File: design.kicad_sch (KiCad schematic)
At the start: 274 parts, among them J1 TYPE-C-31-M-12, U1 TTP223, U10 ATtiny1616-M, U2 TTP223, U3 TTP223, U4 TTP223, U5 TTP223, U6 TTP223, U7 TTP223, U8 TTP223, U9 MAX77751CEFG_T

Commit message: new layout
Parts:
- removed D301, D302, D303, D304, D305, D306, D307, D308, D309, D310, D311, D312, D313, D314, D315, D316, D317, D318, D319, D320, D321, D322, D323, D324, D325, D326, D327, D328, D329, D330, D331, D332, D333, D334, D335, D336, D337, D338, D339, D340, D341, D342, D343, D344, D345, D346, D347, D348, D349, D350, D351, D352, D353, D354, D355, D356, D357, D358, D359, D360, D361, D362, D363, D364, D365, D366, D367, D368, D369, D370, D371, D372, D373, D374, D375, D376, D377, D378, D379, D380, D381, D382, D383, D384, D385, D386, D387, D388, D389, D390, D391, D392, D393, D394, D395, D396: WS2812B, LED_SMD:LED_WS2812B_PLCC4_5.0x5.0mm_P3.2mm, symbol LED:WS2812B

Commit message: updates
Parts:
- added J301: TYPE-C-31-M-12, Snapeda:TYPE-C-31-M-12_HRO_TYPE-C-31-M-12, symbol Snapeda:TYPE-C-31-M-12
- added R301, R302: 5.1k, Resistor_SMD:R_0805_2012Metric, symbol Device:R_Small
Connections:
- net +5V: now also J301.A4_B9 (VBUS), J301.B4_A9 (VBUS)
- net GND: now also J301.A1_B12 (GND), J301.B1_A12 (GND), R301.1, R302.2
- net in: now also U10.5 (PA4); no longer U10.1 (PA2)
- net touch_point_1: no longer U10.7 (PA6)
- net touch_point_2: no longer U10.8 (PA7)
- net touch_point_3: no longer U10.14 (PB0)
- net touch_point_4: no longer U10.13 (PB1)
- net touch_point_5: no longer U10.12 (PB2)
- net touch_point_6: no longer U10.11 (PB3)
- net touch_point_7: no longer U10.10 (PB4)
- net touch_point_8: no longer U10.9 (PB5)
- net touch_state_1: now also U10.18 (PC3)
- net touch_state_2: now also U10.17 (PC2)
- net touch_state_3: now also U10.16 (PC1)
- net touch_state_4: now also U10.15 (PC0)
- net touch_state_5: now also U10.11 (PB3)
- net touch_state_6: now also U10.10 (PB4)
- net touch_state_7: now also U10.9 (PB5)
- net touch_state_8: now also U10.8 (PA7)
- net at R9.1: now also U10.6 (PA5); no longer U10.15 (PC0)
- net at R10.1: now also U10.7 (PA6); no longer U10.16 (PC1)
- new net: J301.A5 (CC1), R301.2
- new net: J301.B5 (CC2), R302.1
- new net: J301.S1 (SHIELD), J301.S2 (SHIELD), J301.S3 (SHIELD), J301.S4 (SHIELD)
- no-connect marks 9 -> 12
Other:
- moved on the sheet: D101, D102, R10, R9

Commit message: upadte
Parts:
- removed C17, C18, C19, C22: 10uF, Capacitor_SMD:C_0805_2012Metric, symbol Device:C_Small
- removed C20, C24, C25: 2.2uF, Capacitor_SMD:C_0805_2012Metric, symbol Device:C_Small
- removed C21: 0.1uF, Capacitor_SMD:C_0805_2012Metric, symbol Device:C_Small
- removed C23: 22uF, Capacitor_SMD:C_0805_2012Metric, symbol Device:C_Small
- removed D100: STAT, LED_SMD:LED_0603_1608Metric, symbol Device:LED_Small
- removed D98: VBUS, LED_SMD:LED_0603_1608Metric, symbol Device:LED_Small
- removed D99: INOKB, LED_SMD:LED_0603_1608Metric, symbol Device:LED_Small
- removed J1: TYPE-C-31-M-12, Snapeda:TYPE-C-31-M-12_HRO_TYPE-C-31-M-12, symbol Snapeda:TYPE-C-31-M-12
- removed JP17: ENBST, LED_SMD:LED_0603_1608Metric, symbol Jumper:Jumper_2_Bridged
- removed L1: 0.47uH, Inductor_SMD:L_0805_2012Metric, symbol Device:L_Small
- removed R2, R3, R5: 1k, Resistor_SMD:R_0805_2012Metric, symbol Device:R_Small
- removed R4, R6: 5.1k, Resistor_SMD:R_0805_2012Metric, symbol Device:R_Small
- removed R7: 2.4k, Resistor_SMD:R_0805_2012Metric, symbol Device:R_Small
- removed R8: 13.3k, Resistor_SMD:R_0805_2012Metric, symbol Device:R_Small
- removed TP10: BAT-, TestPoint:TestPoint_Pad_4.0x4.0mm, symbol Connector:TestPoint
- removed TP9: BAT+, TestPoint:TestPoint_Pad_4.0x4.0mm, symbol Connector:TestPoint
- removed U9: MAX77751CEFG_T, Snapeda:IC_MAX77751CEFG_T, symbol Snapeda:MAX77751CEFG_T
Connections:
- no-connect marks 12 -> 9
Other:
- note removed: "If ENBST is driven high, the reverse boost is enabled and the BYP-to-CHGIN path is closed. internall pulldown"
- note removed: "RESISTANCE (kΩ) IFAST (mA) 2.4 500 RTOPOFF (kΩ) ITOPOFF (mA) 13.3 200"
- moved on the sheet: D97, R1

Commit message: added lcsc number test
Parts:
- D1: LCSC (none) -> C123456
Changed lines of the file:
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@@
       (effects (font (size 1.27 1.27)) (justify left top) hide)
+    )
+    (property "LCSC" "C123456" (id 4) (at 369.57 41.91 0)
+      (effects (font (size 1.27 1.27)) hide)
     )
     (pin "1")

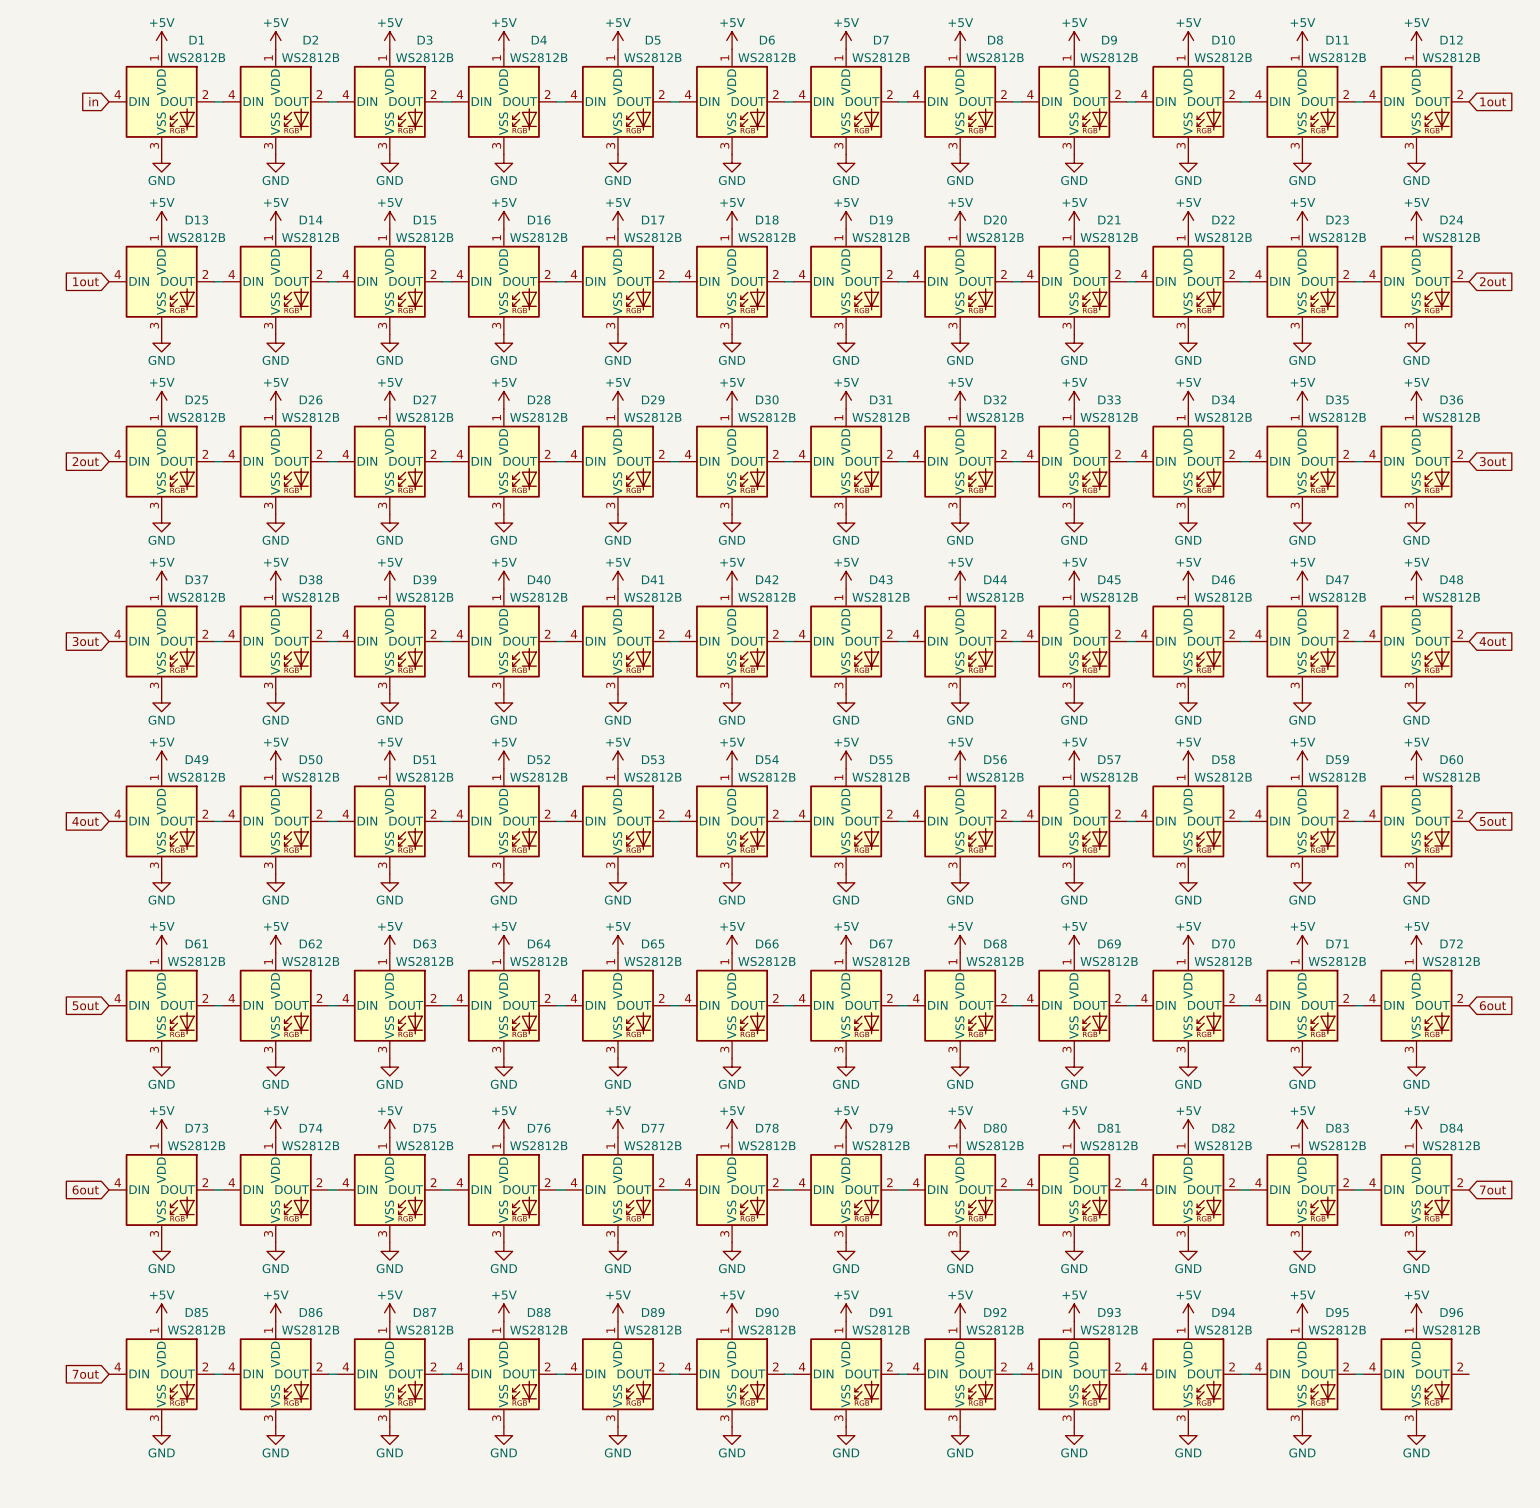
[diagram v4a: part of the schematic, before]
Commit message: update all LEDs with LCSC #
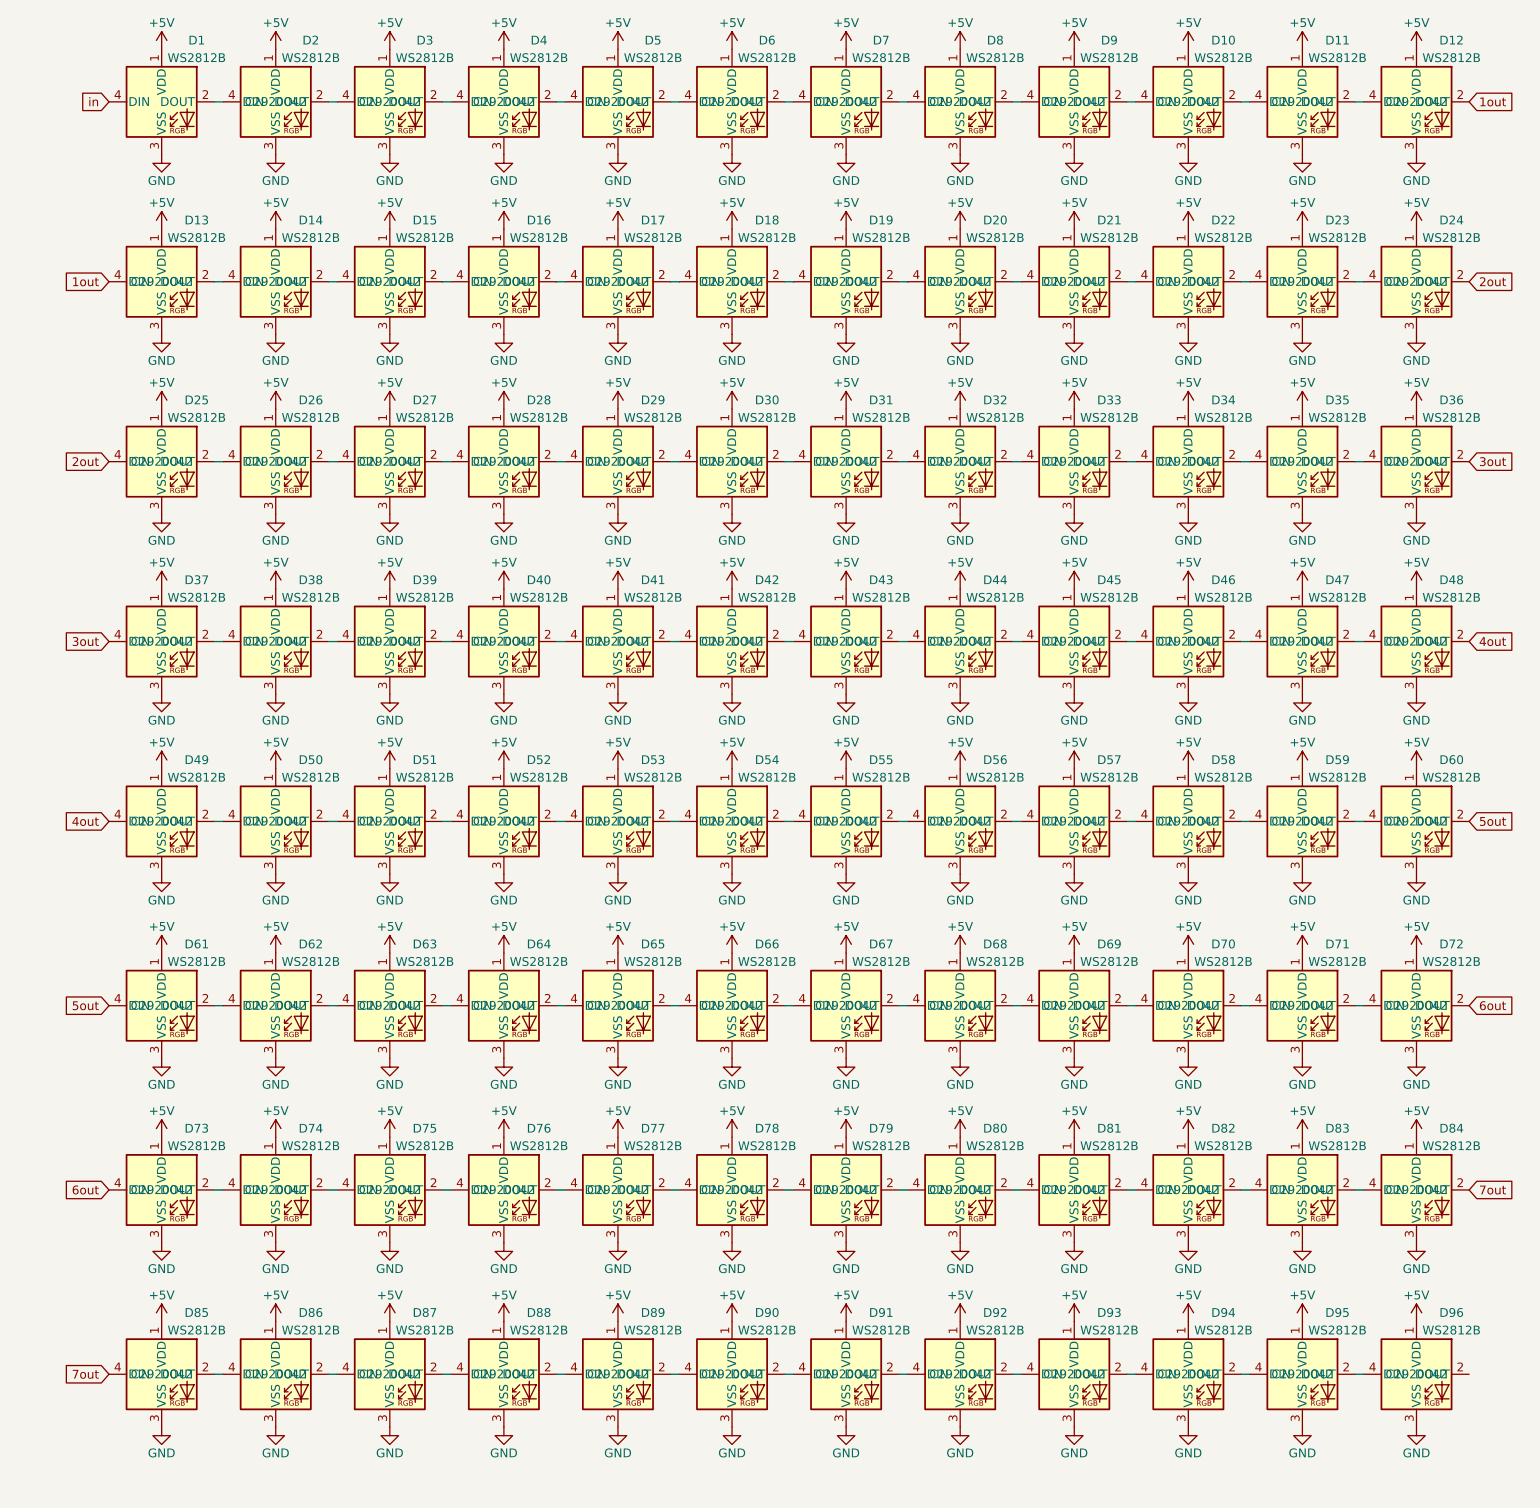
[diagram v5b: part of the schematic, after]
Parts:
- D1: LCSC C123456 -> C2920042
- D10, D11, D12, D13, D14, D15, D16, D17, D18, D19, D2, D20, D21, D22, D23, D24, D25, D26, D27, D28, D29, D3, D30, D31, D32, D33, D34, D35, D36, D37, D38, D39, D4, D40, D41, D42, D43, D44, D45, D46, D47, D48, D49, D5, D50, D51, D52, D53, D54, D55, D56, D57, D58, D59, D6, D60, D61, D62, D63, D64, D65, D66, D67, D68, D69, D7, D70, D71, D72, D73, D74, D75, D76, D77, D78, D79, D8, D80, D81, D82, D83, D84, D85, D86, D87, D88, D89, D9, D90, D91, D92, D93, D94, D95, D96: LCSC (none) -> C2920042

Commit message: update
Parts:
- added TP301: UPDI, TestPoint:TestPoint_Pad_3.0x3.0mm, symbol Connector:TestPoint
- added TP302: +5V, TestPoint:TestPoint_Pad_3.0x3.0mm, symbol Connector:TestPoint
- added TP303: GND, TestPoint:TestPoint_Pad_3.0x3.0mm, symbol Connector:TestPoint
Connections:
- net +5V: now also TP302.1
- net GND: now also TP303.1
- net UPDI: now also TP301.1
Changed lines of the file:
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@@
     (stroke (width 0) (type default) (color 0 0 0 0))
   )
+  (wire (pts (xy 485.14 292.735) (xy 485.14 295.275))
+    (stroke (width 0) (type default) (color 0 0 0 0))
+  )
   (wire (pts (xy 459.74 41.91) (xy 461.01 41.91))
     (stroke (width 0) (type default) (color 0 0 0 0))
@@
     (stroke (width 0) (type default) (color 0 0 0 0))
   )
+  (wire (pts (xy 469.265 292.735) (xy 469.265 295.275))
+    (stroke (width 0) (type default) (color 0 0 0 0))
+  )
   (wire (pts (xy 245.11 197.485) (xy 245.11 189.23))
     (stroke (width 0) (type default) (color 0 0 0 0))
@@
     (stroke (width 0) (type default) (color 0 0 0 0))
   )
+  (wire (pts (xy 469.265 295.275) (xy 474.98 295.275))
+    (stroke (width 0) (type default) (color 0 0 0 0))
+  )
   (wire (pts (xy 151.13 325.12) (xy 151.13 334.01))
     (stroke (width 0) (type default) (color 0 0 0 0))
@@
     (stroke (width 0) (type default) (color 0 0 0 0))
   )
+  (wire (pts (xy 474.98 295.275) (xy 474.98 292.735))
+    (stroke (width 0) (type default) (color 0 0 0 0))
+  )
   (wire (pts (xy 410.21 226.06) (xy 411.48 226.06))
     (stroke (width 0) (type default) (color 0 0 0 0))
@@
     )
   )
+  (global_label "UPDI" (shape input) (at 459.105 292.735 270) (fields_autoplaced)
+    (effects (font (size 1.27 1.27)) (justify right))
+    (property "Referenzen zwischen Schaltplänen" "${INTERSHEET_REFS}" (id 0) (at 459.0256 299.5344 90)
+      (effects (font (size 1.27 1.27)) (justify right) hide)
+    )
+  )
   (global_label "touch_point_6" (shape input) (at 170.18 299.72 0) (fields_autoplaced)
     (effects (font (size 1.27 1.27)) (justify left))
@@
     (pin "1")
   )
+  (symbol (lib_id "power:+5V") (at 469.265 292.735 0) (unit 1)
+    (in_bom yes) (on_board yes) (fields_autoplaced)
+    (property "Reference" "#PWR0234" (id 0) (at 469.265 296.545 0)
+      (effects (font (size 1.27 1.27)) hide)
+    )
+    (property "Value" "+5V" (id 1) (at 469.265 287.02 0))
+    (property "Footprint" "" (id 2) (at 469.265 292.735 0)
+      (effects (font (size 1.27 1.27)) hide)
+    )
+    (property "Datasheet" "" (id 3) (at 469.265 292.735 0)
+      (effects (font (size 1.27 1.27)) hide)
+    )
+    (pin "1")
+  )
   (symbol (lib_name "WS2812B_64") (lib_id "LED:WS2812B") (at 452.12 226.06 0) (unit 1)
     (in_bom yes) (on_board yes)
@@
     (pin "1")
   )
+  (symbol (lib_id "Connector:TestPoint") (at 474.98 292.735 0) (unit 1)
+    (in_bom yes) (on_board yes) (fields_autoplaced)
+    (property "Reference" "TP302" (id 0) (at 477.52 288.1629 0)
+      (effects (font (size 1.27 1.27)) (justify left))
+    )
+    (property "Value" "+5V" (id 1) (at 477.52 290.7029 0)
+      (effects (font (size 1.27 1.27)) (justify left))
+    )
+    (property "Footprint" "TestPoint:TestPoint_Pad_3.0x3.0mm" (id 2) (at 480.06 292.735 0)
+      (effects (font (size 1.27 1.27)) hide)
+    )
+    (property "Datasheet" "~" (id 3) (at 480.06 292.735 0)
+      (effects (font (size 1.27 1.27)) hide)
+    )
+    (pin "1")
+  )
   (symbol (lib_name "WS2812B_89") (lib_id "LED:WS2812B") (at 518.16 146.05 0) (unit 1)
     (in_bom yes) (on_board yes)
@@
     (pin "4")
   )
+  (symbol (lib_id "Connector:TestPoint") (at 485.14 292.735 0) (unit 1)
+    (in_bom yes) (on_board yes) (fields_autoplaced)
+    (property "Reference" "TP303" (id 0) (at 487.045 288.1629 0)
+      (effects (font (size 1.27 1.27)) (justify left))
+    )
+    (property "Value" "GND" (id 1) (at 487.045 290.7029 0)
+      (effects (font (size 1.27 1.27)) (justify left))
+    )
+    (property "Footprint" "TestPoint:TestPoint_Pad_3.0x3.0mm" (id 2) (at 490.22 292.735 0)
+      (effects (font (size 1.27 1.27)) hide)
+    )
+    (property "Datasheet" "~" (id 3) (at 490.22 292.735 0)
+      (effects (font (size 1.27 1.27)) hide)
+    )
+    (pin "1")
+  )
   (symbol (lib_id "power:GND") (at 137.16 322.58 0) (unit 1)
     (in_bom yes) (on_board yes) (fields_autoplaced)
@@
     (pin "1")
   )
+  (symbol (lib_id "Connector:TestPoint") (at 459.105 292.735 0) (unit 1)
+    (in_bom yes) (on_board yes) (fields_autoplaced)
+    (property "Reference" "TP301" (id 0) (at 461.645 288.1629 0)
+      (effects (font (size 1.27 1.27)) (justify left))
+    )
+    (property "Value" "UPDI" (id 1) (at 461.645 290.7029 0)
+      (effects (font (size 1.27 1.27)) (justify left))
+    )
+    (property "Footprint" "TestPoint:TestPoint_Pad_3.0x3.0mm" (id 2) (at 464.185 292.735 0)
+      (effects (font (size 1.27 1.27)) hide)
+    )
+    (property "Datasheet" "~" (id 3) (at 464.185 292.735 0)
+      (effects (font (size 1.27 1.27)) hide)
+    )
+    (pin "1")
+  )
   (symbol (lib_id "power:GND") (at 501.65 180.34 0) (unit 1)
     (in_bom yes) (on_board yes)
@@
     (pin "4")
   )
+  (symbol (lib_id "power:GND") (at 485.14 295.275 0) (unit 1)
+    (in_bom yes) (on_board yes) (fields_autoplaced)
+    (property "Reference" "#PWR0236" (id 0) (at 485.14 301.625 0)
+      (effects (font (size 1.27 1.27)) hide)
+    )
+    (property "Value" "GND" (id 1) (at 487.045 296.5449 0)
+      (effects (font (size 1.27 1.27)) (justify left))
+    )
+    (property "Footprint" "" (id 2) (at 485.14 295.275 0)
+      (effects (font (size 1.27 1.27)) hide)
+    )
+    (property "Datasheet" "" (id 3) (at 485.14 295.275 0)
+      (effects (font (size 1.27 1.27)) hide)
+    )
+    (pin "1")
+  )
   (symbol (lib_name "WS2812B_27") (lib_id "LED:WS2812B") (at 419.1 199.39 0) (unit 1)
     (in_bom yes) (on_board yes)
@@
       (reference "#PWR0233") (unit 1) (value "+5V") (footprint "")
     )
+    (path "/4c9bdd78-2042-4cab-9994-7ab1fa74e901"
+      (reference "#PWR0234") (unit 1) (value "+5V") (footprint "")
+    )
     (path "/20eca63c-90e6-4032-aac9-6261fc70c0a9"
       (reference "#PWR0235") (unit 1) (value "GND") (footprint "")
     )
+    (path "/ec532ca6-7037-47bc-ad25-0a3366bf9412"
+      (reference "#PWR0236") (unit 1) (value "GND") (footprint "")
+    )
     (path "/6eb54f31-fab6-4d9a-8844-a45c1f2771a0"
       (reference "#PWR0251") (unit 1) (value "+5V") (footprint "")
@@
       (reference "TP8") (unit 1) (value "touch_point_2") (footprint "")
     )
+    (path "/c807062e-e916-48ff-a5d1-108afea6de1c"
+      (reference "TP301") (unit 1) (value "UPDI") (footprint "TestPoint:TestPoint_Pad_3.0x3.0mm")
+    )
+    (path "/77b6fa1c-9085-4bba-9177-f62eb3d50273"
+      (reference "TP302") (unit 1) (value "+5V") (footprint "TestPoint:TestPoint_Pad_3.0x3.0mm")
+    )
+    (path "/c38522eb-924c-434d-8c4d-b709a146463b"
+      (reference "TP303") (unit 1) (value "GND") (footprint "TestPoint:TestPoint_Pad_3.0x3.0mm")
+    )
     (path "/bfcab283-22f5-4984-b0ea-81ccb74a5155"
